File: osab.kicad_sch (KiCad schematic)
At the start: 97 parts, among them CON1 TF-01A, CON2 PJ-3420-A-SMT, CON3 TYPE-C-31-M-12, Q1 BC847B, Q2 BC847B, SW1 PPP, SW10 RESET, SW11 Torch, SW2 VOL-, SW3 VOL+, SW4 CHAP-, SW5 CHAP+, SW6 OT/NT, SW7 BOOK-, SW8 BOOK+, SW9 XKB5858-Z-F, U1 VS1000, U2 ME6211C33M5G-N, U3 CAT25640, U4 TP4055, U5 MF5853CS, U6 PAM8302AAS, Y1 12MHz

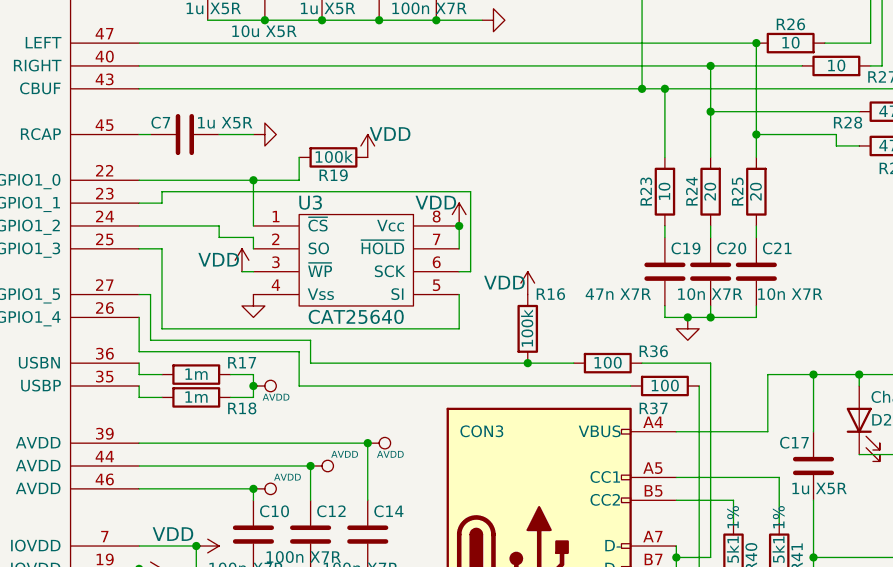
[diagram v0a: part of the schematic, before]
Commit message: production: Added C26 for eeprom; routing tracks
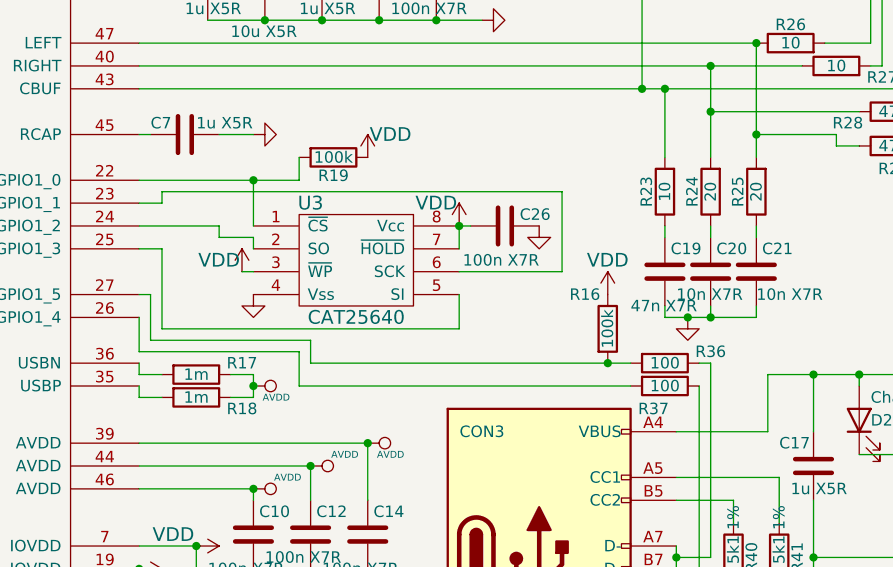
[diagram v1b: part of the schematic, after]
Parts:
- added C26: 100n X7R, Capacitor_SMD:C_0603_1608Metric, symbol Device:C
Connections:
- net GND: now also C26.2
- net VDD: now also C26.1
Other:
- moved on the sheet: R16, R36
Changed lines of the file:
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@@
   (junction (at 144.78 73.66) (diameter 0) (color 0 0 0 0)
   )
+  (junction (at 182.88 111.76) (diameter 0) (color 0 0 0 0)
+  )
   (junction (at 21.59 123.19) (diameter 0) (color 0 0 0 0)
   )
@@
   (junction (at 144.78 60.96) (diameter 0) (color 0 0 0 0)
   )
-  (junction (at 173.99 111.76) (diameter 0) (color 0 0 0 0)
-  )
   (junction (at 48.26 76.2) (diameter 0) (color 0 0 0 0)
   )
@@
     (stroke (width 0) (type default) (color 0 0 0 0))
   )
+  (wire (pts (xy 166.37 96.52) (xy 167.64 96.52))
+    (stroke (width 0) (type default) (color 0 0 0 0))
+  )
   (wire (pts (xy 78.74 83.82) (xy 73.66 83.82))
     (stroke (width 0) (type default) (color 0 0 0 0))
@@
     (stroke (width 0) (type default) (color 0 0 0 0))
   )
-  (wire (pts (xy 167.64 101.6) (xy 167.64 92.71))
+  (wire (pts (xy 177.8 101.6) (xy 177.8 92.71))
     (stroke (width 0) (type default) (color 0 0 0 0))
   )
@@
     (stroke (width 0) (type default) (color 0 0 0 0))
   )
-  (wire (pts (xy 167.64 92.71) (xy 133.35 92.71))
+  (wire (pts (xy 133.35 92.71) (xy 177.8 92.71))
     (stroke (width 0) (type default) (color 0 0 0 0))
   )
@@
     (stroke (width 0) (type default) (color 0 0 0 0))
   )
-  (wire (pts (xy 173.99 111.76) (xy 179.07 111.76))
+  (wire (pts (xy 149.86 111.76) (xy 182.88 111.76))
     (stroke (width 0) (type default) (color 0 0 0 0))
   )
@@
     (stroke (width 0) (type default) (color 0 0 0 0))
   )
-  (wire (pts (xy 186.69 111.76) (xy 194.31 111.76))
-    (stroke (width 0) (type default) (color 0 0 0 0))
-  )
   (wire (pts (xy 53.34 129.54) (xy 53.34 125.73))
     (stroke (width 0) (type default) (color 0 0 0 0))
@@
     (stroke (width 0) (type default) (color 0 0 0 0))
   )
-  (wire (pts (xy 149.86 111.76) (xy 173.99 111.76))
-    (stroke (width 0) (type default) (color 0 0 0 0))
-  )
   (wire (pts (xy 41.91 152.4) (xy 39.37 152.4))
     (stroke (width 0) (type default) (color 0 0 0 0))
@@
     (stroke (width 0) (type default) (color 0 0 0 0))
   )
-  (wire (pts (xy 166.37 101.6) (xy 167.64 101.6))
+  (wire (pts (xy 166.37 101.6) (xy 177.8 101.6))
     (stroke (width 0) (type default) (color 0 0 0 0))
   )
@@
     (stroke (width 0) (type default) (color 0 0 0 0))
   )
+  (wire (pts (xy 193.04 111.76) (xy 194.31 111.76))
+    (stroke (width 0) (type default) (color 0 0 0 0))
+  )
   (wire (pts (xy 191.77 106.68) (xy 194.31 106.68))
     (stroke (width 0) (type default) (color 0 0 0 0))
@@
     (stroke (width 0) (type default) (color 0 0 0 0))
   )
+  (wire (pts (xy 182.88 111.76) (xy 185.42 111.76))
+    (stroke (width 0) (type default) (color 0 0 0 0))
+  )
   (wire (pts (xy 132.08 41.91) (xy 134.62 41.91))
     (stroke (width 0) (type default) (color 0 0 0 0))
@@
       (effects (font (size 1.27 1.27)) (justify left))
     )
-    (property "Value" "47n X7R" (id 1) (at 180.34 104.14 0)
+    (property "Value" "47n X7R" (id 1) (at 185.42 105.41 0)
       (effects (font (size 1.27 1.27)) (justify left))
     )
@@
     (pin "2")
   )
-  (symbol (lib_id "Device:R") (at 173.99 107.95 0) (unit 1)
+  (symbol (lib_id "Device:R") (at 182.88 107.95 0) (unit 1)
     (in_bom yes) (on_board yes)
-    (property "Reference" "R16" (id 0) (at 176.53 104.14 0))
-    (property "Value" "100k" (id 1) (at 173.99 107.95 90))
-    (property "Footprint" "Resistor_SMD:R_0603_1608Metric" (id 2) (at 172.212 107.95 90)
+    (property "Reference" "R16" (id 0) (at 180.34 104.14 0))
+    (property "Value" "100k" (id 1) (at 182.88 107.95 90))
+    (property "Footprint" "Resistor_SMD:R_0603_1608Metric" (id 2) (at 181.102 107.95 90)
       (effects (font (size 1.27 1.27)) hide)
     )
-    (property "Datasheet" "https://datasheet.lcsc.com/lcsc/1811091512_Viking-Tech-ARG03FTC1003_C217682.pdf" (id 3) (at 173.99 107.95 0)
+    (property "Datasheet" "https://datasheet.lcsc.com/lcsc/1811091512_Viking-Tech-ARG03FTC1003_C217682.pdf" (id 3) (at 182.88 107.95 0)
       (effects (font (size 1.27 1.27)) hide)
     )
-    (property "3D-model" "Included in KiCad" (id 4) (at 173.99 107.95 0)
+    (property "3D-model" "Included in KiCad" (id 4) (at 182.88 107.95 0)
       (effects (font (size 1.27 1.27)) hide)
     )
-    (property "Link" "https://lcsc.com/product-detail/Chip-Resistor-Surface-Mount_Viking-Tech-ARG03FTC1003_C217682.html" (id 5) (at 173.99 107.95 0)
+    (property "Link" "https://lcsc.com/product-detail/Chip-Resistor-Surface-Mount_Viking-Tech-ARG03FTC1003_C217682.html" (id 5) (at 182.88 107.95 0)
       (effects (font (size 1.27 1.27)) hide)
     )
-    (property "MPN" "ARG03FTC1003" (id 6) (at 173.99 107.95 0)
+    (property "MPN" "ARG03FTC1003" (id 6) (at 182.88 107.95 0)
       (effects (font (size 1.27 1.27)) hide)
     )
@@
     (pin "2")
   )
-  (symbol (lib_id "Device:R") (at 182.88 111.76 270) (unit 1)
+  (symbol (lib_id "Device:R") (at 189.23 111.76 270) (unit 1)
     (in_bom yes) (on_board yes)
-    (property "Reference" "R36" (id 0) (at 187.96 110.49 90))
-    (property "Value" "100" (id 1) (at 182.88 111.76 90))
-    (property "Footprint" "Resistor_SMD:R_0603_1608Metric" (id 2) (at 182.88 109.982 90)
+    (property "Reference" "R36" (id 0) (at 194.31 110.49 90))
+    (property "Value" "100" (id 1) (at 189.23 111.76 90))
+    (property "Footprint" "Resistor_SMD:R_0603_1608Metric" (id 2) (at 189.23 109.982 90)
       (effects (font (size 1.27 1.27)) hide)
     )
-    (property "Datasheet" "https://datasheet.lcsc.com/lcsc/1811091620_Viking-Tech-ARG03FTC1000_C217683.pdf" (id 3) (at 182.88 111.76 0)
+    (property "Datasheet" "https://datasheet.lcsc.com/lcsc/1811091620_Viking-Tech-ARG03FTC1000_C217683.pdf" (id 3) (at 189.23 111.76 0)
       (effects (font (size 1.27 1.27)) hide)
     )
-    (property "3D-model" "Included in KiCad" (id 4) (at 182.88 111.76 0)
+    (property "3D-model" "Included in KiCad" (id 4) (at 189.23 111.76 0)
       (effects (font (size 1.27 1.27)) hide)
     )
-    (property "Link" "https://lcsc.com/product-detail/Chip-Resistor-Surface-Mount_Viking-Tech-ARG03FTC1000_C217683.html" (id 5) (at 182.88 111.76 0)
+    (property "Link" "https://lcsc.com/product-detail/Chip-Resistor-Surface-Mount_Viking-Tech-ARG03FTC1000_C217683.html" (id 5) (at 189.23 111.76 0)
       (effects (font (size 1.27 1.27)) hide)
     )
-    (property "MPN" "ARG03FTC1000" (id 6) (at 182.88 111.76 0)
+    (property "MPN" "ARG03FTC1000" (id 6) (at 189.23 111.76 0)
       (effects (font (size 1.27 1.27)) hide)
     )
@@
     (pin "2")
   )
-  (symbol (lib_id "power:VDD") (at 173.99 104.14 0) (unit 1)
+  (symbol (lib_id "power:VDD") (at 182.88 104.14 0) (unit 1)
     (in_bom yes) (on_board yes)
-    (property "Reference" "#PWR0103" (id 0) (at 173.99 107.95 0)
+    (property "Reference" "#PWR0103" (id 0) (at 182.88 107.95 0)
       (effects (font (size 1.524 1.524)) hide)
     )
-    (property "Value" "VDD" (id 1) (at 171.45 102.87 0)
+    (property "Value" "VDD" (id 1) (at 182.88 100.33 0)
       (effects (font (size 1.524 1.524)))
     )
-    (property "Footprint" "" (id 2) (at 173.99 104.14 0)
+    (property "Footprint" "" (id 2) (at 182.88 104.14 0)
       (effects (font (size 1.524 1.524)))
     )
-    (property "Datasheet" "" (id 3) (at 173.99 104.14 0)
+    (property "Datasheet" "" (id 3) (at 182.88 104.14 0)
       (effects (font (size 1.524 1.524)))
     )
     (pin "1")
   )
+  (symbol (lib_id "Device:C") (at 171.45 96.52 90) (unit 1)
+    (in_bom yes) (on_board yes)
+    (property "Reference" "C26" (id 0) (at 176.53 95.25 90)
+      (effects (font (size 1.27 1.27)) (justify left))
+    )
+    (property "Value" "100n X7R" (id 1) (at 175.26 100.33 90)
+      (effects (font (size 1.27 1.27)) (justify left))
+    )
+    (property "Footprint" "Capacitor_SMD:C_0603_1608Metric" (id 2) (at 175.26 95.5548 0)
+      (effects (font (size 1.27 1.27)) hide)
+    )
+    (property "Datasheet" "https://datasheet.lcsc.com/lcsc/1811021431_Samsung-Electro-Mechanics-CL10B104KB8NNNC_C1591.pdf" (id 3) (at 171.45 96.52 0)
+      (effects (font (size 1.27 1.27)) hide)
+    )
+    (property "3D-model" "Included in KiCad" (id 4) (at 171.45 96.52 0)
+      (effects (font (size 1.27 1.27)) hide)
+    )
+    (property "Link" "https://lcsc.com/product-detail/Multilayer-Ceramic-Capacitors-MLCC-SMD-SMT_Samsung-Electro-Mechanics-CL10B104KB8NNNC_C1591.html" (id 5) (at 171.45 96.52 0)
+      (effects (font (size 1.27 1.27)) hide)
+    )
+    (property "MPN" "CL10B104KB8NNNC" (id 6) (at 171.45 96.52 0)
+      (effects (font (size 1.27 1.27)) hide)
+    )
+    (pin "1")
+    (pin "2")
+  )
   (symbol (lib_id "power:GND") (at 273.05 90.17 0) (unit 1)
     (in_bom yes) (on_board yes)
@@
     (pin "2")
   )
+  (symbol (lib_id "power:GND") (at 175.26 96.52 0) (unit 1)
+    (in_bom yes) (on_board yes)
+    (property "Reference" "#PWR038" (id 0) (at 175.26 102.87 0)
+      (effects (font (size 1.524 1.524)) hide)
+    )
+    (property "Value" "GND" (id 1) (at 175.26 101.6 0)
+      (effects (font (size 1.524 1.524)) hide)
+    )
+    (property "Footprint" "" (id 2) (at 175.26 96.52 0)
+      (effects (font (size 1.524 1.524)))
+    )
+    (property "Datasheet" "" (id 3) (at 175.26 96.52 0)
+      (effects (font (size 1.524 1.524)))
+    )
+    (pin "1")
+  )
   (symbol (lib_id "Device:R") (at 137.16 115.57 270) (unit 1)
     (in_bom yes) (on_board yes)
@@
       (reference "#PWR037") (unit 1) (value "GND") (footprint "")
     )
+    (path "/77176c54-ebb1-4c8b-8fdb-57a742f16efb"
+      (reference "#PWR038") (unit 1) (value "GND") (footprint "")
+    )
     (path "/00000000-0000-0000-0000-000054d422bd"
       (reference "#PWR039") (unit 1) (value "VDD") (footprint "")
@@
       (reference "C25") (unit 1) (value "220p C0G") (footprint "Capacitor_SMD:C_0603_1608Metric")
     )
+    (path "/206e6c98-56d6-441f-afab-7cffb4c54223"
+      (reference "C26") (unit 1) (value "100n X7R") (footprint "Capacitor_SMD:C_0603_1608Metric")
+    )
     (path "/00000000-0000-0000-0000-00005e145bc9"

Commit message: production: Added LCSC references
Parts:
- BATTERY1: LCSC (none) -> C2688784
- C1, C2: LCSC (none) -> C1653
- C10, C12, C14, C15, C16, C26, C6, C8: LCSC (none) -> C1591
- C11, C18, C3: LCSC (none) -> C19702
- C13, C17, C23, C4, C5, C7, C9: LCSC (none) -> C15849
- C19: LCSC (none) -> C1622
- C20, C21: LCSC (none) -> C1589
- C22: LCSC (none) -> C1613
- C24, C25: LCSC (none) -> C27675
- CON1: LCSC (none) -> C91145
- CON2: LCSC (none) -> C319102
- CON3: LCSC (none) -> C165948
- D1: LCSC (none) -> C375469
- D2: LCSC (none) -> C125114
- FB1, FB2: LCSC (none) -> C275454
- Q1, Q2: LCSC (none) -> C94393
- R1, R10, R12, R15, R16, R19, R22: LCSC (none) -> C217682
- R11, R14, R2, R3, R31, R34, R38, R4, R5, R6, R7, R8: LCSC (none) -> C217687
- R13, R20, R30, R32, R35: LCSC (none) -> C217840
- R17, R18, R9: LCSC (none) -> C234360
- R21, R40, R41: LCSC (none) -> C218090
- R23, R26, R27: LCSC (none) -> C217691
- R24, R25: LCSC (none) -> C217873
- R28, R29: LCSC (none) -> C218042
- R33: LCSC (none) -> C217971
- R36, R37: LCSC (none) -> C217683
- R39: LCSC (none) -> C23154
- SW1, SW10, SW11, SW2, SW3, SW4, SW5, SW6, SW7, SW8: LCSC (none) -> C92584
- SW9: LCSC (none) -> C780036
- U1: LCSC (none) -> C486305
- U2: LCSC (none) -> C82942
- U3: LCSC (none) -> C153776
- U4: LCSC (none) -> C28441
- U5: LCSC (none) -> C375698
- U6: LCSC (none) -> C113367
- Y1: LCSC (none) -> C9002

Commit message: production: Added footprint for speaker connector
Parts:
- SPEAKER1: footprint Connector_JST:JST_GH_SM02B-GHS-TB_1x02-1MP_P1.25mm_Horizontal -> OSAB:HYCW02-WF02-125B
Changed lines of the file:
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@@
   (title_block
     (title "OSAB - the Open Source Audio Bible player")
-    (date "2022-06-03")
+    (date "2022-06-04")
     (rev "7")
     (company "theaudiobible.org")
@@
       (effects (font (size 1.27 1.27)) (justify left) hide)
     )
-    (property "Footprint" "Connector_JST:JST_GH_SM02B-GHS-TB_1x02-1MP_P1.25mm_Horizontal" (id 2) (at 276.86 78.74 0)
+    (property "Footprint" "OSAB:HYCW02-WF02-125B" (id 2) (at 276.86 78.74 0)
       (effects (font (size 1.27 1.27)) hide)
     )
@@
     )
     (path "/00000000-0000-0000-0000-00005e03f86a"
-      (reference "SPEAKER1") (unit 1) (value "Conn_01x02") (footprint "Connector_JST:JST_GH_SM02B-GHS-TB_1x02-1MP_P1.25mm_Horizontal")
+      (reference "SPEAKER1") (unit 1) (value "Conn_01x02") (footprint "OSAB:HYCW02-WF02-125B")
     )
     (path "/00000000-0000-0000-0000-0000543f883c"

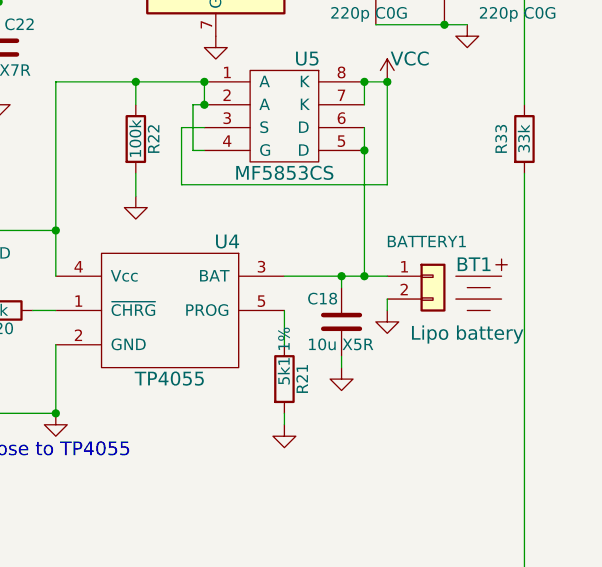
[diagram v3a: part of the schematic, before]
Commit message: production: Corrected battery polarity
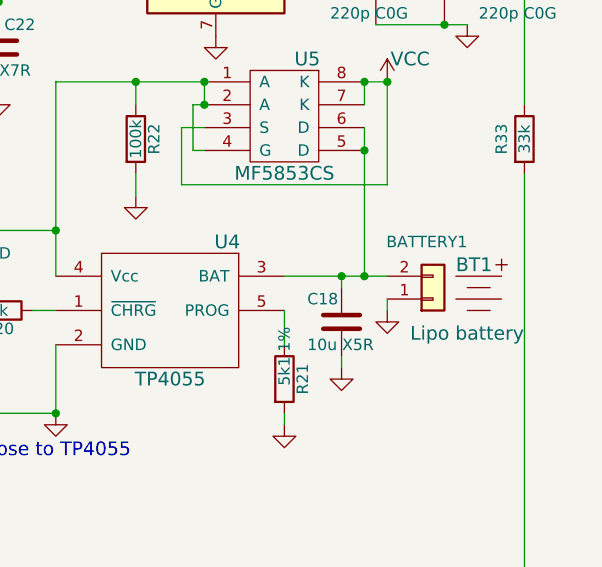
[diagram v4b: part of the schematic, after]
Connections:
- net GND: now also BATTERY1.1 (Pin_1); no longer BATTERY1.2 (Pin_2)
- net at C18.1, U4.3 (BAT), U5.5 (D)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: now also BATTERY1.2 (Pin_2); no longer BATTERY1.1 (Pin_1)
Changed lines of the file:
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@@
     (stroke (width 0) (type default) (color 0 0 0 0))
   )
-  (wire (pts (xy 264.16 120.65) (xy 264.16 121.92))
-    (stroke (width 0) (type default) (color 0 0 0 0))
-  )
   (wire (pts (xy 133.35 93.98) (xy 130.81 93.98))
     (stroke (width 0) (type default) (color 0 0 0 0))
@@
     (stroke (width 0) (type default) (color 0 0 0 0))
   )
+  (wire (pts (xy 261.62 118.11) (xy 264.16 118.11))
+    (stroke (width 0) (type default) (color 0 0 0 0))
+  )
   (wire (pts (xy 149.86 123.19) (xy 149.86 127))
     (stroke (width 0) (type default) (color 0 0 0 0))
@@
     (stroke (width 0) (type default) (color 0 0 0 0))
   )
+  (wire (pts (xy 264.16 120.65) (xy 264.16 121.92))
+    (stroke (width 0) (type default) (color 0 0 0 0))
+  )
   (wire (pts (xy 243.84 99.06) (xy 242.57 99.06))
     (stroke (width 0) (type default) (color 0 0 0 0))
@@
     (stroke (width 0) (type default) (color 0 0 0 0))
   )
-  (wire (pts (xy 264.16 118.11) (xy 261.62 118.11))
-    (stroke (width 0) (type default) (color 0 0 0 0))
-  )
   (wire (pts (xy 71.12 101.6) (xy 78.74 101.6))
     (stroke (width 0) (type default) (color 0 0 0 0))
@@
     (pin "1")
   )
-  (symbol (lib_id "Connector_Generic:Conn_01x02") (at 269.24 118.11 0) (unit 1)
+  (symbol (lib_id "Connector_Generic:Conn_01x02") (at 269.24 120.65 0) (mirror x) (unit 1)
     (in_bom yes) (on_board yes)
     (property "Reference" "BATTERY1" (id 0) (at 273.05 114.3 0)
       (effects (font (size 1.27 1.27)) (justify right))
     )
-    (property "Value" "Conn_01x02" (id 1) (at 271.272 120.6246 0)
+    (property "Value" "Conn_01x02" (id 1) (at 271.272 118.1354 0)
       (effects (font (size 1.27 1.27)) (justify left) hide)
     )
-    (property "Footprint" "Connector_JST:JST_PH_S2B-PH-SM4-TB_1x02-1MP_P2.00mm_Horizontal" (id 2) (at 269.24 118.11 0)
+    (property "Footprint" "Connector_JST:JST_PH_S2B-PH-SM4-TB_1x02-1MP_P2.00mm_Horizontal" (id 2) (at 269.24 120.65 0)
       (effects (font (size 1.27 1.27)) hide)
     )
-    (property "Datasheet" "https://datasheet.lcsc.com/lcsc/2106070035_Shenzhen-Kinghelm-Elec-KH-A2001WF-02A_C2688784.pdf" (id 3) (at 269.24 118.11 0)
+    (property "Datasheet" "https://datasheet.lcsc.com/lcsc/2106070035_Shenzhen-Kinghelm-Elec-KH-A2001WF-02A_C2688784.pdf" (id 3) (at 269.24 120.65 0)
       (effects (font (size 1.27 1.27)) hide)
     )
-    (property "Link" "https://lcsc.com/product-detail/Wire-To-Board-Wire-To-Wire-Connector_Shenzhen-Kinghelm-Elec-KH-A2001WF-02A_C2688784.html" (id 5) (at 269.24 118.11 0)
+    (property "Link" "https://lcsc.com/product-detail/Wire-To-Board-Wire-To-Wire-Connector_Shenzhen-Kinghelm-Elec-KH-A2001WF-02A_C2688784.html" (id 5) (at 269.24 120.65 0)
       (effects (font (size 1.27 1.27)) hide)
     )
-    (property "MPN" "KH-A2001WF-02A" (id 6) (at 269.24 118.11 0)
+    (property "MPN" "KH-A2001WF-02A" (id 6) (at 269.24 120.65 0)
       (effects (font (size 1.27 1.27)) hide)
     )
-    (property "LCSC" "C2688784" (id 7) (at 269.24 118.11 0)
+    (property "LCSC" "C2688784" (id 7) (at 269.24 120.65 0)
       (effects (font (size 1.524 1.524)) hide)
     )
